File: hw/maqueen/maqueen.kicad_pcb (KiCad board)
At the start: 2 copper layers, 80 x 75 mm, 29 parts, among them IC1 MSP430FR2355TPT, J1 conn_DFrobot, J2 ESP01, J3 SBW, SW1 RST, U1 LMV324, Y1 Crystal

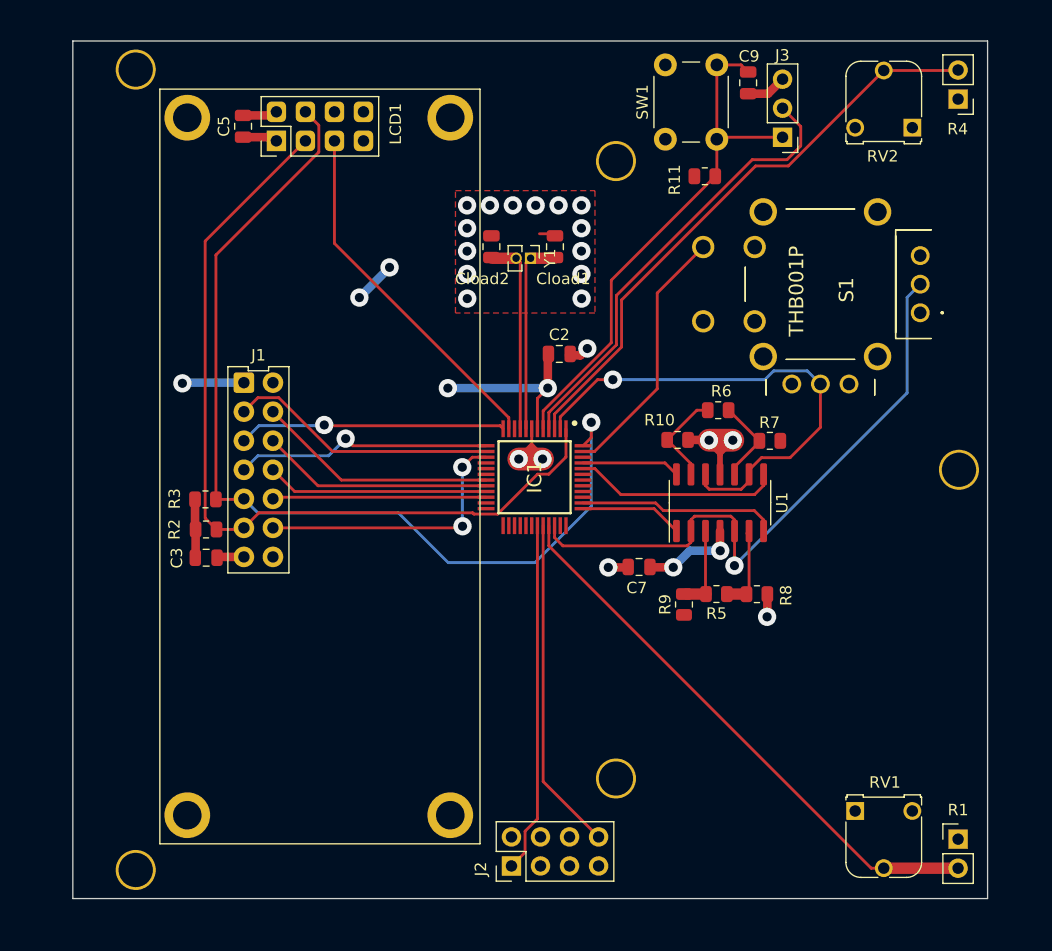
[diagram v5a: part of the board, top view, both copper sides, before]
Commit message: tot drc be, menys huellas i serigrafia
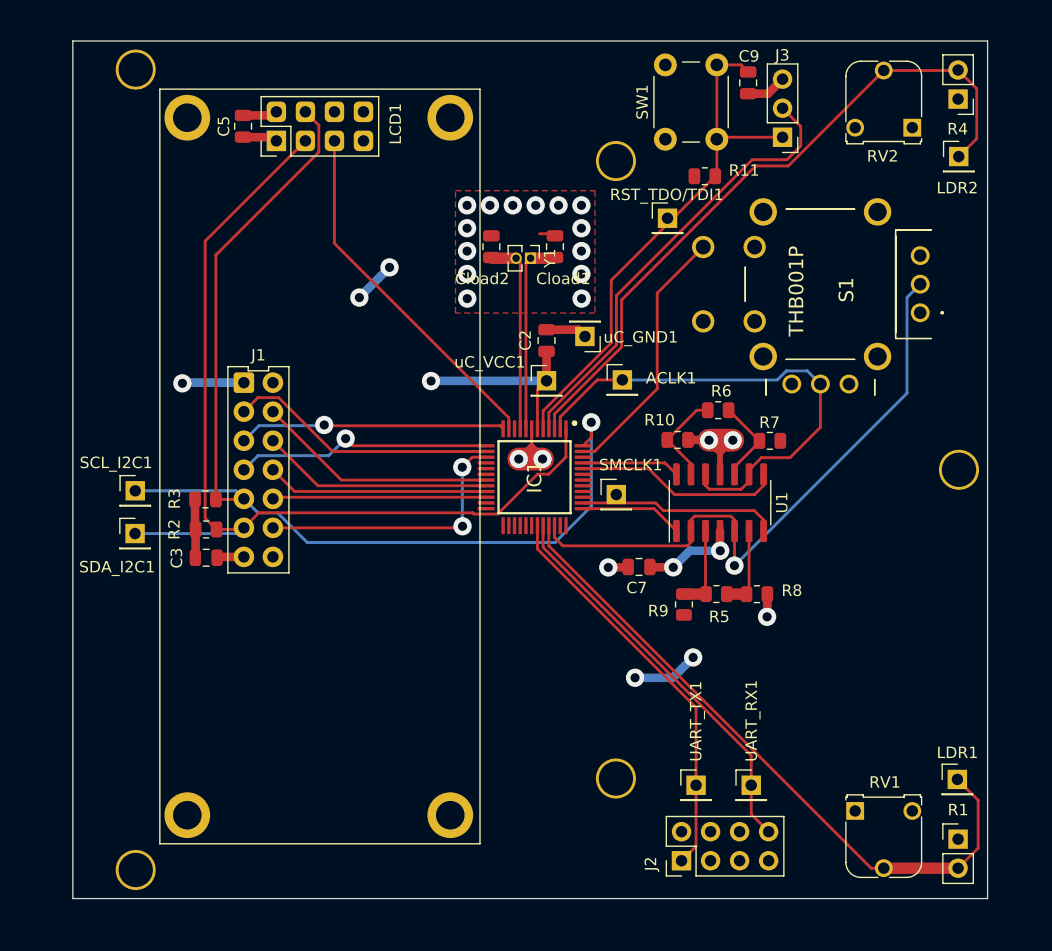
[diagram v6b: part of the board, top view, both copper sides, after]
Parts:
- added ACLK1: ~, Connector_PinHeader_2.54mm:PinHeader_1x01_P2.54mm_Vertical, F.Cu at (157.6, 92.1)
- added LDR1: ~, Connector_PinHeader_2.54mm:PinHeader_1x01_P2.54mm_Vertical, F.Cu at (186.9, 127.0)
- added LDR2: ~, Connector_PinHeader_2.54mm:PinHeader_1x01_P2.54mm_Vertical, F.Cu at (187.1, 72.5)
- added RST_TDO/TDI1: ~, Connector_PinHeader_2.54mm:PinHeader_1x01_P2.54mm_Vertical, F.Cu at (161.6, 77.9)
- added SCL_I2C1: ~, Connector_PinHeader_2.54mm:PinHeader_1x01_P2.54mm_Vertical, F.Cu at (115.0, 101.8)
- added SDA_I2C1: ~, Connector_PinHeader_2.54mm:PinHeader_1x01_P2.54mm_Vertical, F.Cu at (115.0, 105.5)
- added SMCLK1: ~, Connector_PinHeader_2.54mm:PinHeader_1x01_P2.54mm_Vertical, F.Cu at (157.1, 102.1)
- added UART_RX1: ~, Connector_PinHeader_2.54mm:PinHeader_1x01_P2.54mm_Vertical, F.Cu at (168.9, 127.5)
- added UART_TX1: ~, Connector_PinHeader_2.54mm:PinHeader_1x01_P2.54mm_Vertical, F.Cu at (164.1, 127.5)
- added uC_GND1: ~, Connector_PinHeader_2.54mm:PinHeader_1x01_P2.54mm_Vertical, F.Cu at (154.4, 88.3)
- added uC_VCC1: ~, Connector_PinHeader_2.54mm:PinHeader_1x01_P2.54mm_Vertical, F.Cu at (151.0, 92.1)
- moved J2 14.9 mm to (162.8, 134.1)
- moved C2 1.62 mm to (151.0, 88.6), turned to 90 degrees
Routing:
- net SDA_I2C: track 73.8 -> 83.5 mm
- net PHOTO1: track 49.2 -> 58.5 mm
- net PHOTO2: track 51.4 -> 60.3 mm
- net SCL_I2C: track 85.0 -> 93.4 mm
- net +3.3V: track 41.4 -> 49.3 mm, vias 7 -> 8
- net /WIFI_UART_RX: track 29.2 -> 34.9 mm
- net /WIFI_UART_TX: track 30.7 -> 35.6 mm
- net GND: track 32.4 -> 34.2 mm, vias 21 -> 20
- net FB_JOYSTICK: vias 1 -> 0

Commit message: minor tweaks
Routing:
- net GND: track 34.2 -> 32.6 mm
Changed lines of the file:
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@@
   (segment (start 163.3825 97.31) (end 165.195 97.31) (width 0.75) (layer "F.Cu") (net 3))
   (segment (start 158.11 108.46) (end 158.15 108.42) (width 0.75) (layer "F.Cu") (net 3))
-  (segment (start 150.3925 79.28) (end 151.9675 79.28) (width 0.25) (layer "F.Cu") (net 3))
   (segment (start 124.47 68.93) (end 127.065 68.93) (width 0.75) (layer "F.Cu") (net 3))
   (segment (start 153.78 87.67) (end 154.37 88.26) (width 0.75) (layer "F.Cu") (net 3))
@@
   (segment (start 187.06 72.53) (end 188.63 70.96) (width 0.25) (layer "F.Cu") (net 42))
   (segment (start 188.63 66.59) (end 187 64.96) (width 0.25) (layer "F.Cu") (net 42))
-  (segment (start 188.76 128.82) (end 188.76 133.005) (width 0.25) (layer "F.Cu") (net 43))
-  (segment (start 186.94 127) (end 188.76 128.82) (width 0.25) (layer "F.Cu") (net 43))
+  (segment (start 188.76 128.82) (end 188.76 133.005) (width 0.5) (layer "F.Cu") (net 43))
+  (segment (start 186.94 127) (end 188.76 128.82) (width 0.5) (layer "F.Cu") (net 43))
   (segment (start 151.21 104.808) (end 151.21 106.573086) (width 0.25) (layer "F.Cu") (net 43))
   (segment (start 180.505 134.765) (end 180.5 134.76) (width 0.25) (layer "F.Cu") (net 43))
@@
   (segment (start 151.21 106.573086) (end 179.401914 134.765) (width 0.25) (layer "F.Cu") (net 43))
   (segment (start 187 134.765) (end 180.505 134.765) (width 1) (layer "F.Cu") (net 43))
-  (segment (start 188.76 133.005) (end 187 134.765) (width 0.25) (layer "F.Cu") (net 43))
+  (segment (start 188.76 133.005) (end 187 134.765) (width 0.5) (layer "F.Cu") (net 43))
   (zone (net 3) (net_name "GND") (layer "F.Cu") (hatch edge 0.5)
     (priority 2)

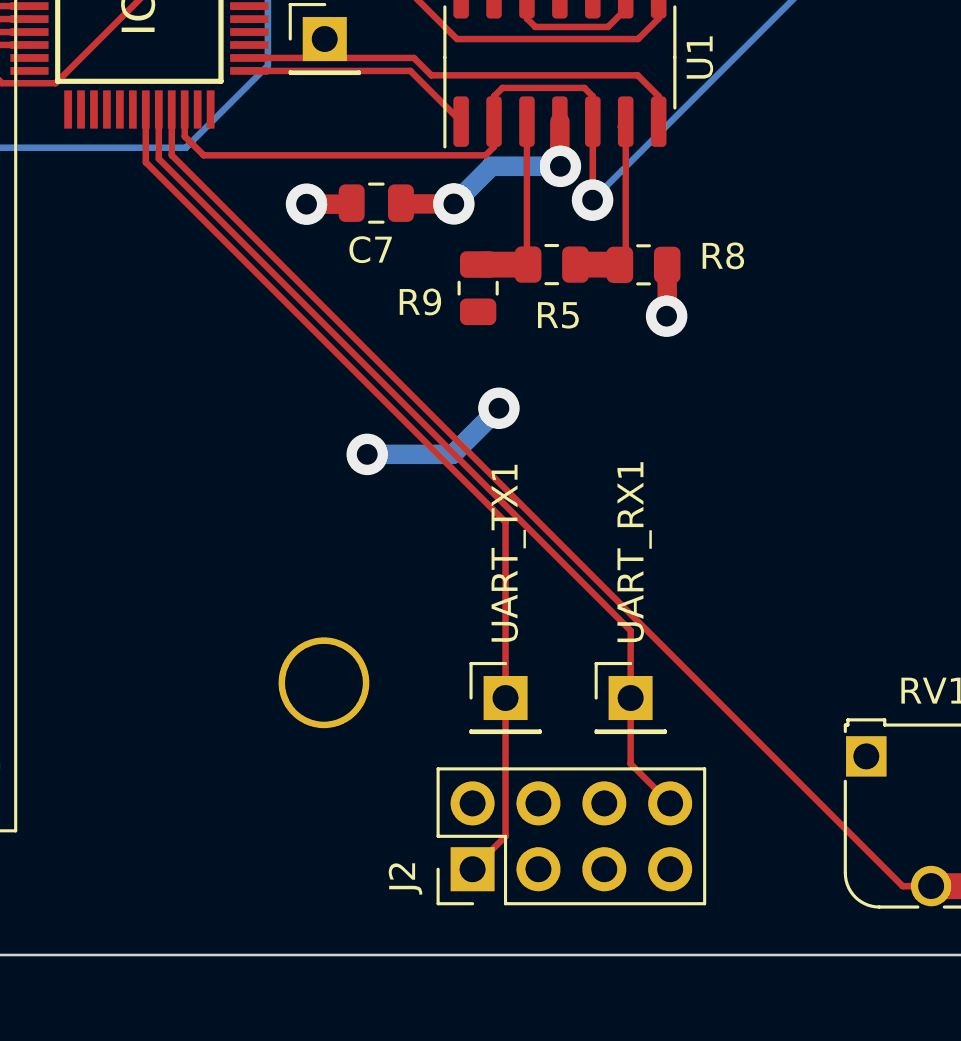
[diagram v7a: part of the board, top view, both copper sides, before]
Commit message: mogut test points del modul wifi als laterals del connector
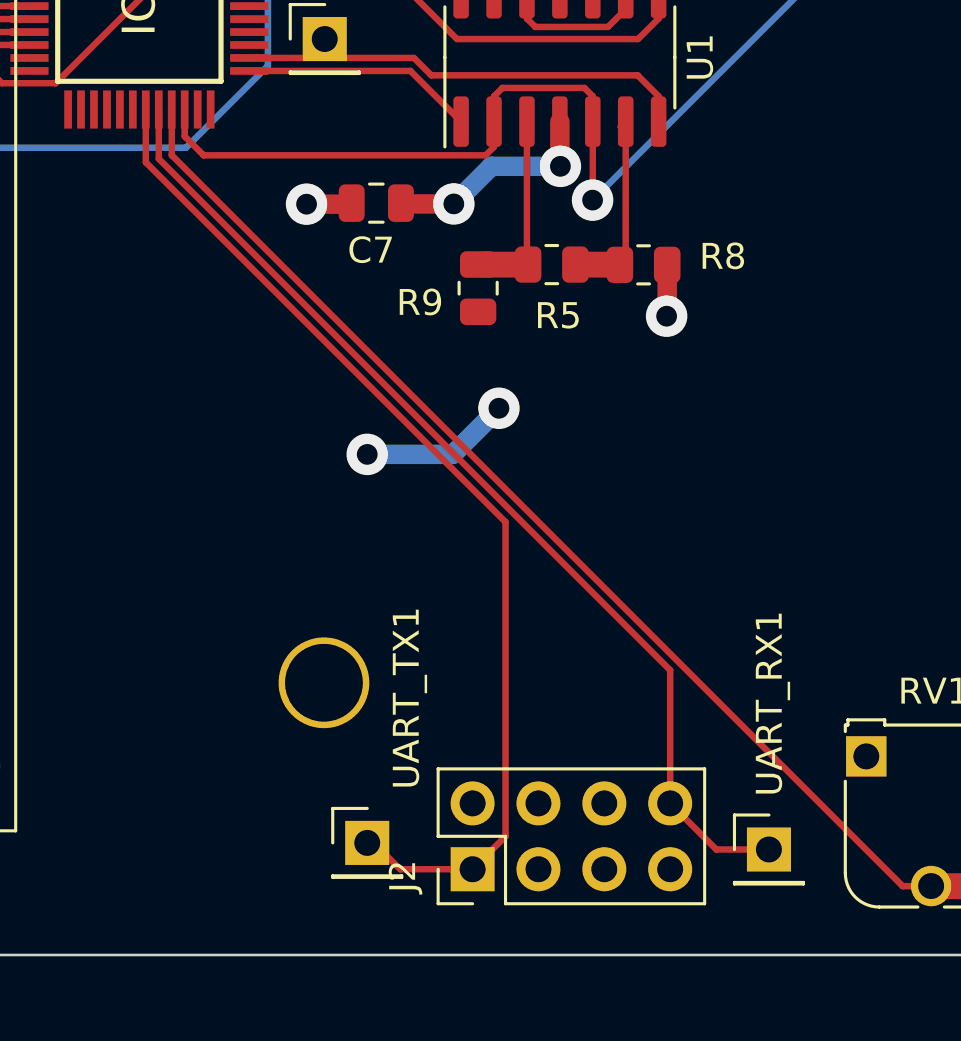
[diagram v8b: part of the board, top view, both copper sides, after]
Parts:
- moved UART_RX1 7.91 mm to (174.2, 133.3)
- moved UART_TX1 7.73 mm to (158.8, 133.1)
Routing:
- net /WIFI_UART_RX: track 34.9 -> 39.5 mm
- net /WIFI_UART_TX: track 35.6 -> 40.1 mm
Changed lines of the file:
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@@
   )
   (footprint "Connector_PinHeader_2.54mm:PinHeader_1x01_P2.54mm_Vertical" (layer "F.Cu")
-    (at 168.91 127.508)
+    (at 174.244 133.35)
     (descr "Through hole straight pin header, 1x01, 2.54mm pitch, single row")
     (tags "Through hole pin header THT 1x01 2.54mm single row")
@@
   )
   (footprint "Connector_PinHeader_2.54mm:PinHeader_1x01_P2.54mm_Vertical" (layer "F.Cu")
-    (at 164.084 127.508)
+    (at 158.75 133.096)
     (descr "Through hole straight pin header, 1x01, 2.54mm pitch, single row")
     (tags "Through hole pin header THT 1x01 2.54mm single row")
@@
     (property "ki_keywords" "test point tp")
     (attr through_hole)
-    (fp_text reference "UART_TX1" (at 0 -5.588 90) (layer "F.SilkS")
+    (fp_text reference "UART_TX1" (at 1.524 -5.588 90) (layer "F.SilkS")
         (effects (font (size 1 1) (thickness 0.15)))
     )
@@
   (segment (start 143.64 99.695) (end 143.64 104.84) (width 0.25) (layer "B.Cu") (net 7))
   (segment (start 143.64 104.84) (end 143.66 104.86) (width 0.25) (layer "B.Cu") (net 7))
-  (segment (start 170.434 131.572) (end 168.91 130.048) (width 0.25) (layer "F.Cu") (net 8))
+  (segment (start 170.434 126.433482) (end 150.71 106.709482) (width 0.25) (layer "F.Cu") (net 8))
+  (segment (start 174.244 133.35) (end 172.212 133.35) (width 0.25) (layer "F.Cu") (net 8))
+  (segment (start 172.212 133.35) (end 170.434 131.572) (width 0.25) (layer "F.Cu") (net 8))
+  (segment (start 170.434 131.572) (end 170.434 126.433482) (width 0.25) (layer "F.Cu") (net 8))
   (segment (start 150.71 106.709482) (end 150.71 104.808) (width 0.25) (layer "F.Cu") (net 8))
-  (segment (start 168.91 124.909482) (end 150.71 106.709482) (width 0.25) (layer "F.Cu") (net 8))
-  (segment (start 168.91 130.048) (end 168.91 124.909482) (width 0.25) (layer "F.Cu") (net 8))
+  (segment (start 159.004 133.096) (end 160.02 134.112) (width 0.25) (layer "F.Cu") (net 9))
+  (segment (start 158.75 133.096) (end 159.004 133.096) (width 0.25) (layer "F.Cu") (net 9))
   (segment (start 162.814 134.112) (end 164.084 132.842) (width 0.25) (layer "F.Cu") (net 9))
+  (segment (start 160.02 134.112) (end 162.814 134.112) (width 0.25) (layer "F.Cu") (net 9))
   (segment (start 164.084 120.719878) (end 150.21 106.845878) (width 0.25) (layer "F.Cu") (net 9))
   (segment (start 150.21 106.845878) (end 150.21 104.808) (width 0.25) (layer "F.Cu") (net 9))
